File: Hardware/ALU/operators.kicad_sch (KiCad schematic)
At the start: 23 parts, among them U1 74LS157, U2 74HC86, U3 74LS283, U4 74151, U5 74151, U6 74151, U7 74151

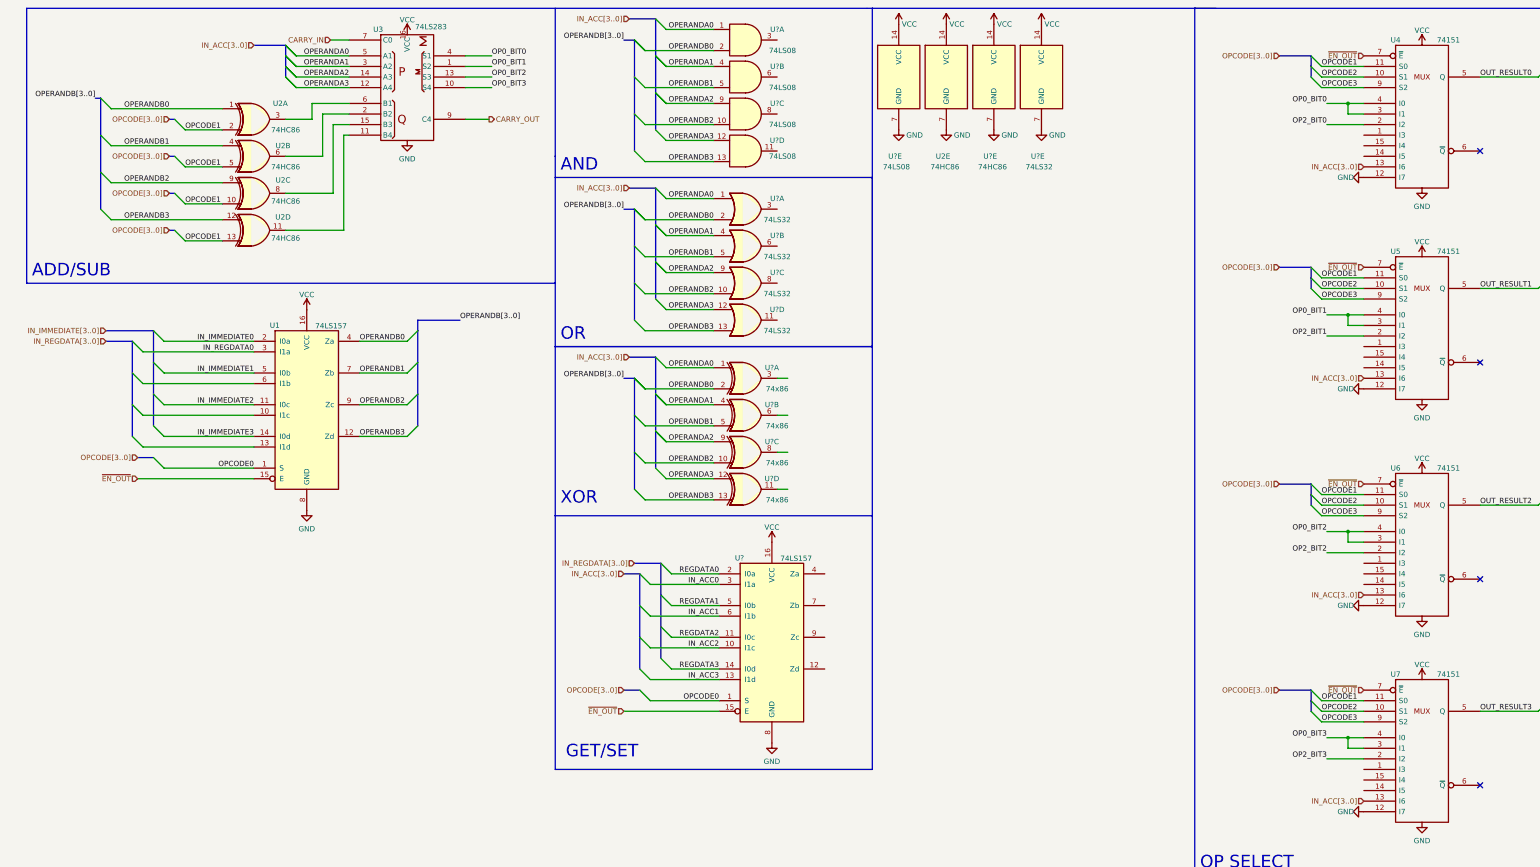
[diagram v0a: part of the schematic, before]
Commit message: ALU Schematic: A backup save before I realized Kicad doesn't seem to officially support hierarchical busses. Soon to replace all sheet busses with lines (I guess four lines isn't too many...)
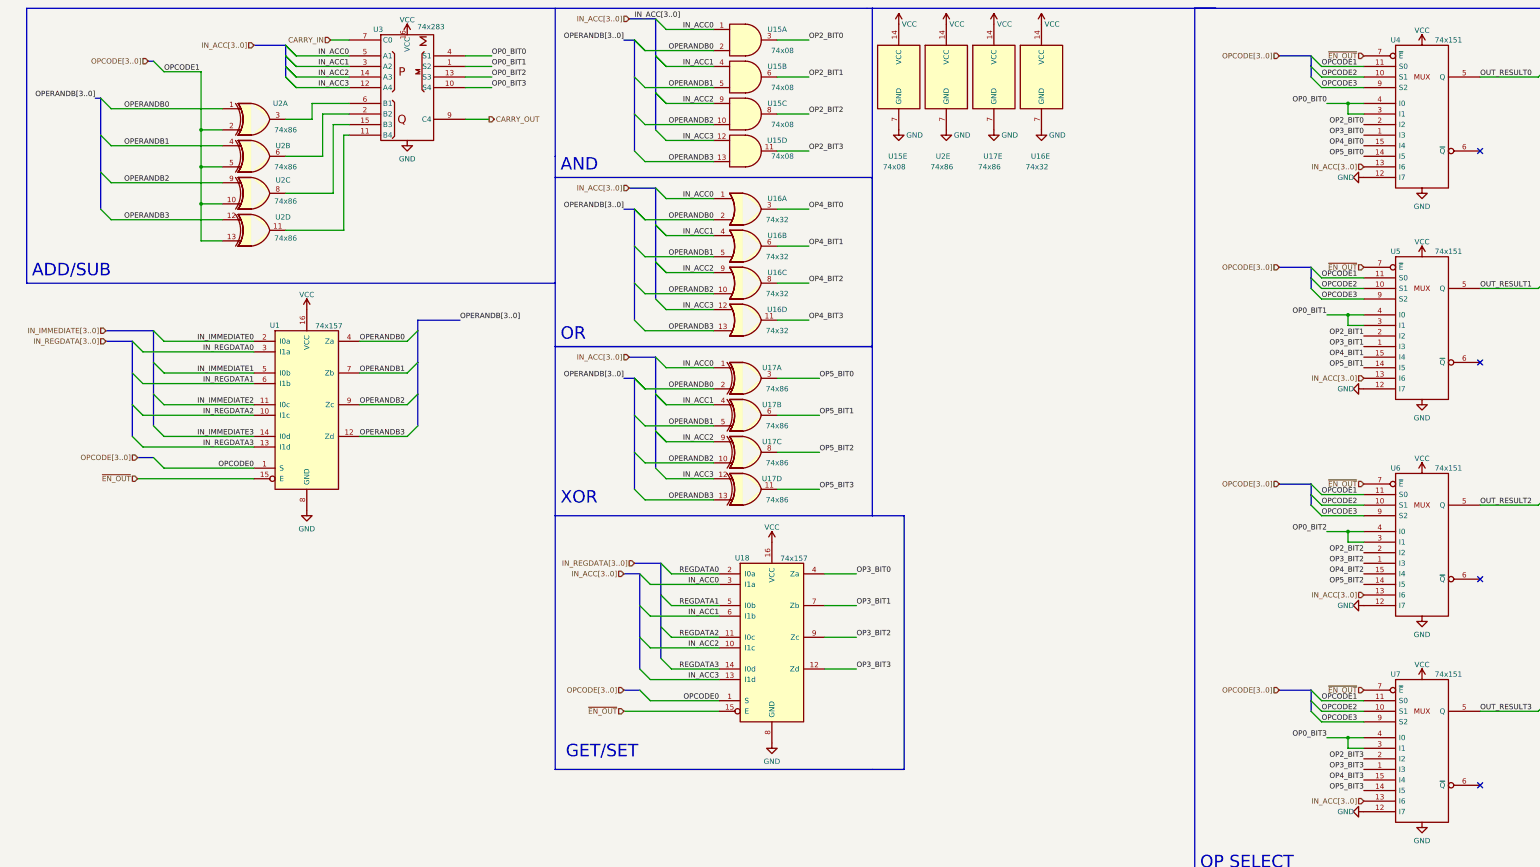
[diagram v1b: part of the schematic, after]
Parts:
- U1: value 74LS157 -> 74x157; footprint (none) -> 000custom:R-PDSO-G16
- U15: renamed from U?; value 74LS08 -> 74x08; footprint (none) -> 000custom:R-PDSO-G16
- U16: renamed from U?; value 74LS32 -> 74x32; footprint (none) -> 000custom:R-PDSO-G16
- U17: renamed from U?; footprint (none) -> 000custom:R-PDSO-G16
- U17: renamed from U?; value 74HC86 -> 74x86; footprint (none) -> 000custom:R-PDSO-G16
- U18: renamed from U?; value 74LS157 -> 74x157; footprint (none) -> 000custom:R-PDSO-G16
- U2: value 74HC86 -> 74x86; footprint (none) -> 000custom:R-PDSO-G16
- U3: value 74LS283 -> 74x283; footprint (none) -> 000custom:R-PDSO-G16
- U4, U5, U6, U7: value 74151 -> 74x151; footprint (none) -> 000custom:R-PDSO-G16
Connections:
- net OPERANDA0 is gone; now on net IN_ACC0: U15.1, U16.1, U17.1, U3.5 (A1)
- net OPERANDA1 is gone; now on net IN_ACC1: U15.4, U16.4, U17.4, U3.3 (A2)
- net OPERANDA2 is gone; now on net IN_ACC2: U15.9, U16.9, U17.9, U3.14 (A3)
- net OPERANDA3 is gone; now on net IN_ACC3: U15.12, U16.12, U17.12, U3.12 (A4)
- net OP2_BIT0: now also U15.3
- net OP2_BIT1: now also U15.6
- net OP2_BIT2: now also U15.8
- net OP2_BIT3: now also U15.11
- net OP3_BIT2: now reaches U6.1 (I3)
- net OP3_BIT2: now also U18.9 (Zc)
- net OP5_BIT2: now reaches U6.14 (I5)
- net OP5_BIT2: now also U17.8
- net OP4_BIT2: now reaches U6.15 (I4)
- net OP4_BIT2: now also U16.8
- net OP5_BIT0: now reaches U17.3
- net OP5_BIT0: now also U4.14 (I5)
- net OP4_BIT0: now reaches U16.3
- net OP4_BIT0: now also U4.15 (I4)
- net OP5_BIT1: now reaches U17.6
- net OP5_BIT1: now also U5.14 (I5)
- net OP3_BIT0: now reaches U4.1 (I3)
- net OP3_BIT0: now also U18.4 (Za)
- net OP4_BIT1: now reaches U16.6
- net OP4_BIT1: now also U5.15 (I4)
- net OP3_BIT3: now reaches U18.12 (Zd)
- net OP3_BIT3: now also U7.1 (I3)
- net OP3_BIT1: now reaches U18.7 (Zb)
- net OP3_BIT1: now also U5.1 (I3)
- net OP4_BIT3: now reaches U16.11
- net OP4_BIT3: now also U7.15 (I4)
- net OP5_BIT3: now reaches U7.14 (I5)
- net OP5_BIT3: now also U17.11
- net IN_REGDATA2: now reaches U1.10 (I1c)
- net IN_REGDATA3: now reaches U1.13 (I1d)
- net IN_REGDATA1: now reaches U1.6 (I1b)

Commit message: ALU: About to increase modularity by moving opcode parsing out of ALU onto motherboard (would turn backplane into more of a motherboard).
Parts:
- U2MUX3: renamed from U1; footprint 000custom:R-PDSO-G16 -> 000custom:D_R-PDSO-G16; stock (none) -> 6; to buy (none) -> 20
- U2MUX4: renamed from U18; footprint 000custom:R-PDSO-G16 -> 000custom:D_R-PDSO-G16; stock (none) -> 6; to buy (none) -> 20
- U8MUX1: renamed from U4; footprint 000custom:R-PDSO-G16 -> 000custom:D_R-PDSO-G16; stock (none) -> 36
- U8MUX2: renamed from U5; footprint 000custom:R-PDSO-G16 -> 000custom:D_R-PDSO-G16; stock (none) -> 36
- U8MUX3: renamed from U6; footprint 000custom:R-PDSO-G16 -> 000custom:D_R-PDSO-G16; stock (none) -> 36
- U8MUX4: renamed from U7; footprint 000custom:R-PDSO-G16 -> 000custom:D_R-PDSO-G16; stock (none) -> 36
- UADD1: renamed from U3; footprint 000custom:R-PDSO-G16 -> 000custom:D_R-PDSO-G16; stock (none) -> 6
- UAND3: renamed from U15; footprint 000custom:R-PDSO-G16 -> 000custom:D_R-PDSO-G14; stock (none) -> 0; to buy (none) -> 20
- UOR2: renamed from U16; footprint 000custom:R-PDSO-G16 -> 000custom:D_R-PDSO-G14; stock (none) -> 0; to buy (none) -> 20
- UXOR2: renamed from U2; footprint 000custom:R-PDSO-G16 -> 000custom:D_R-PDSO-G14; stock (none) -> 9; to buy (none) -> 20
- UXOR3: renamed from U17; footprint 000custom:R-PDSO-G16 -> 000custom:D_R-PDSO-G14; stock (none) -> 9; to buy (none) -> 20
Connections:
- net IN_ACC1 is gone; now on net GND: U2MUX4.6 (I1b), UADD1.3 (A2), UAND3.4, UOR2.4, UXOR3.4
- net REGDATA0 is gone; now on net IN_REGDATA0: U2MUX4.2 (I0a)
- net REGDATA1 is gone; now on net IN_REGDATA1: U2MUX4.5 (I0b)
- net REGDATA2 is gone; now on net IN_REGDATA2: U2MUX4.11 (I0c)
- net REGDATA3 is gone; now on net IN_REGDATA3: U2MUX4.14 (I0d)
- net GND: now also U8MUX1.13 (I6), U8MUX2.13 (I6), U8MUX3.13 (I6), U8MUX4.13 (I6)
- net IN_ACC[3..0]: no longer U8MUX1.13 (I6), U8MUX2.13 (I6), U8MUX3.13 (I6), U8MUX4.13 (I6)
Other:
- note added: "Busses can't easily enter/leave hierarchical sheets"
- note added: "Is this an IMM instruction or a REG instruction?"
- note added: "TODO why the heck is this causing errors"
- moved on the sheet: U2MUX3, U2MUX4, UADD1, UAND3A, UAND3B, UAND3C, UAND3D, UAND3E, UOR2A, UOR2B, UOR2C, UOR2D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

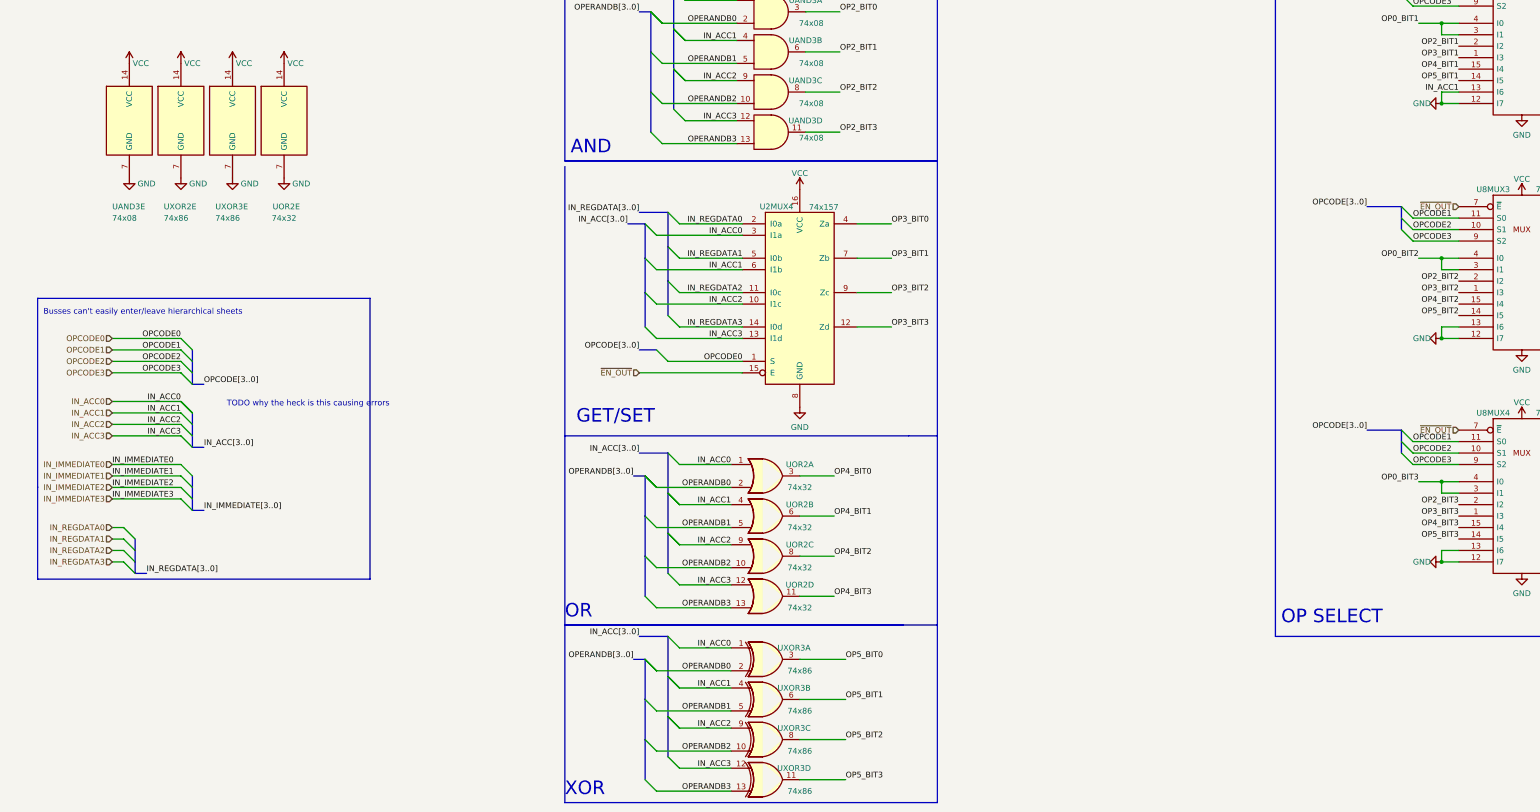
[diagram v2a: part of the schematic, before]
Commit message: ALU: Starting routing. Also passing this to kicad's github #collab
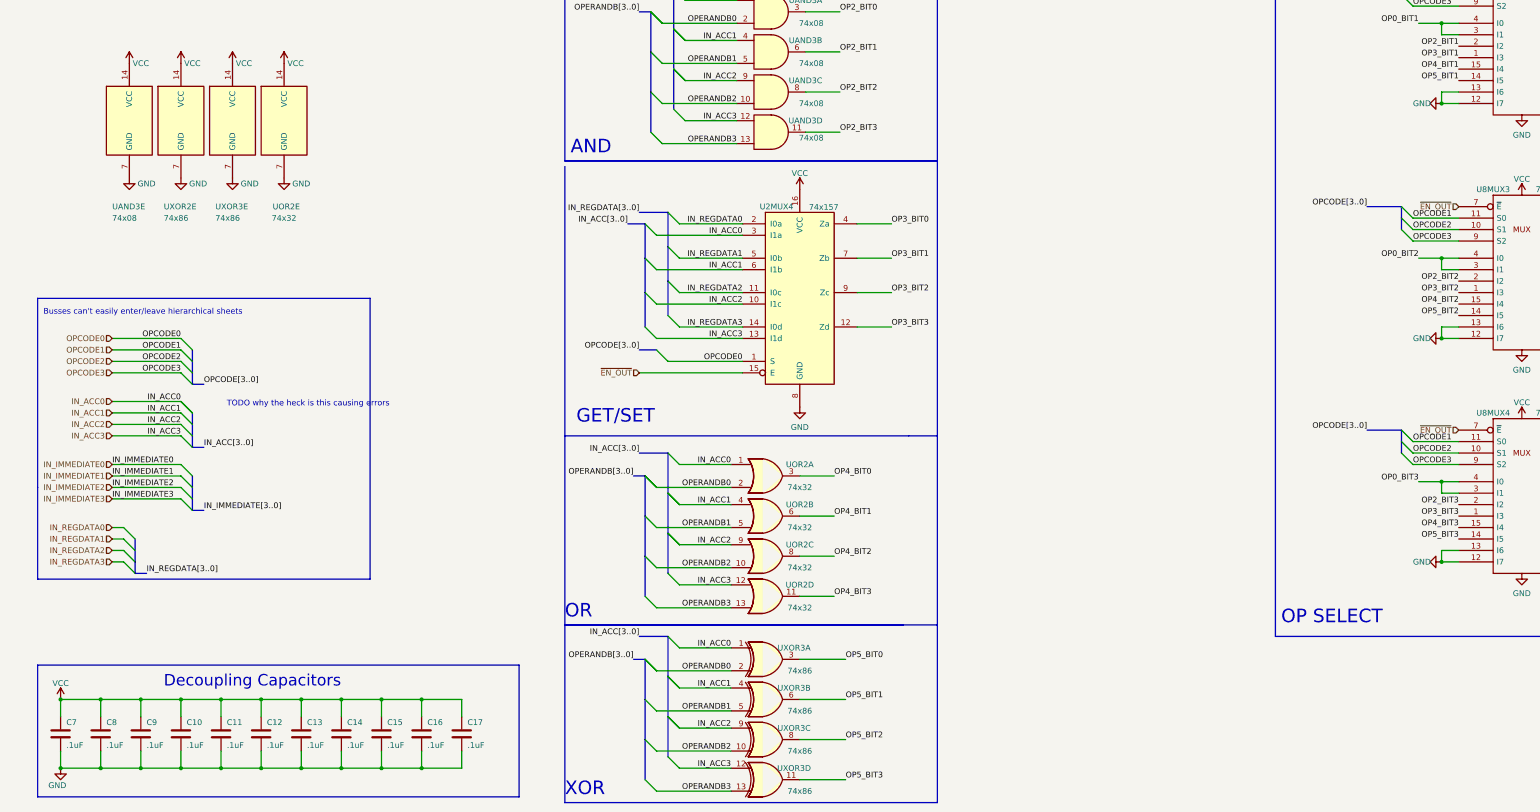
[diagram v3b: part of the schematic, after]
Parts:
- added C10, C11, C12, C13, C14, C15, C16, C17, C7, C8, C9: .1uF, Capacitor_SMD:C_1206_3216Metric_Pad1.33x1.80mm_HandSolder, symbol Device:C
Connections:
- net GND: now also C10.2, C11.2, C12.2, C13.2, C14.2, C15.2, C16.2, C17.2, C7.2, C8.2, C9.2; no longer U2MUX4.6 (I1b), UADD1.3 (A2), UAND3.4, UOR2.4, UXOR3.4
- net VCC: now also C10.1, C11.1, C12.1, C13.1, C14.1, C15.1, C16.1, C17.1, C7.1, C8.1, C9.1
- new net IN_ACC1: U2MUX4.6 (I1b), UADD1.3 (A2), UAND3.4, UOR2.4, UXOR3.4
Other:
- note added: "Decoupling Capacitors"
